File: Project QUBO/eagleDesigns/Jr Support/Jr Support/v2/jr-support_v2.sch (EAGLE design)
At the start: 254 parts, among them IC1 74LVC1G08DBV, IC2 TLC2272PW, IC3 74LVC1G08DBV, IC4 74LVC1G08DBV, Q1 FDN5618P, U1 PCA9685, U2 LT3063, U3 LT3063

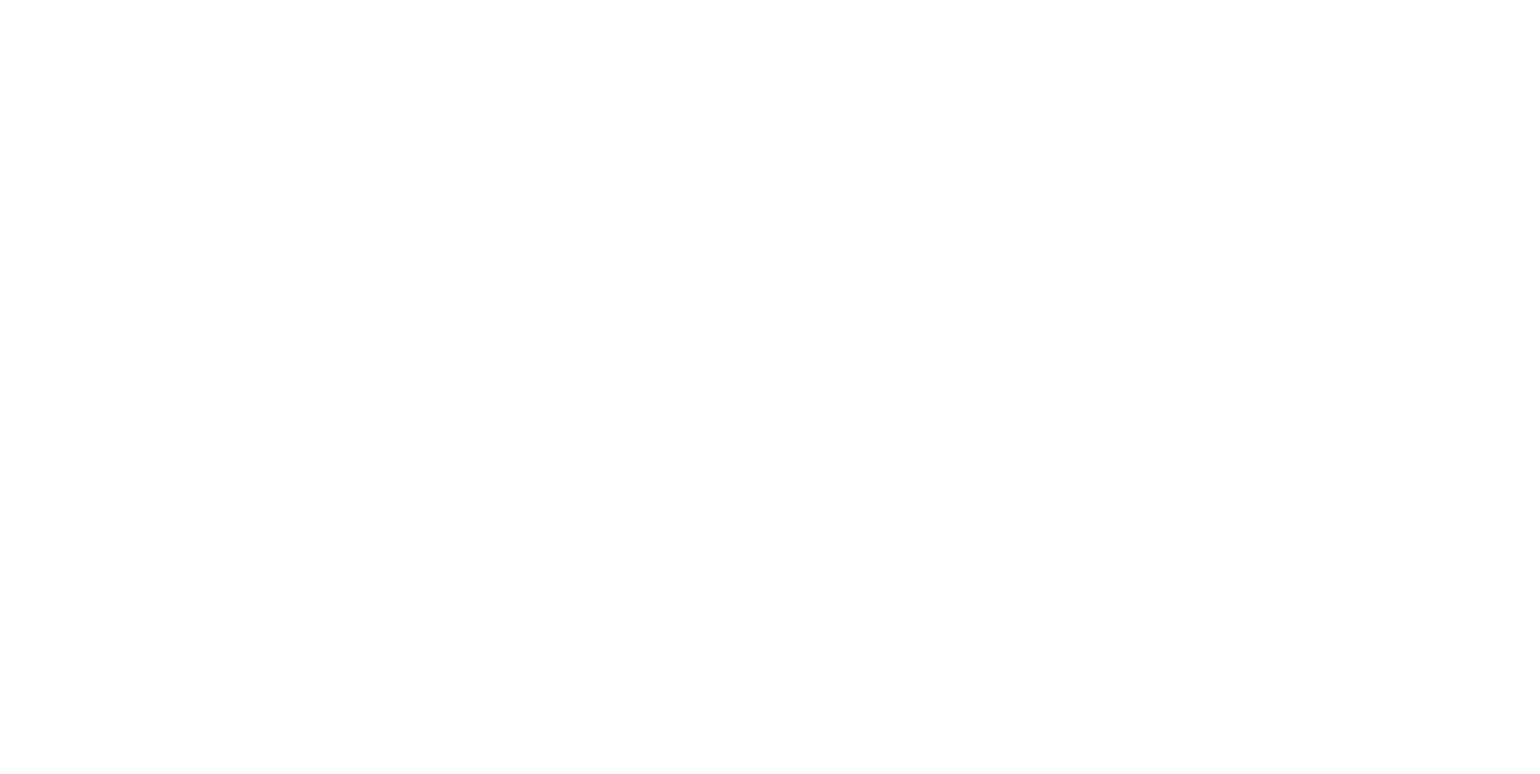
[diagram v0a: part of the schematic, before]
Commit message: 
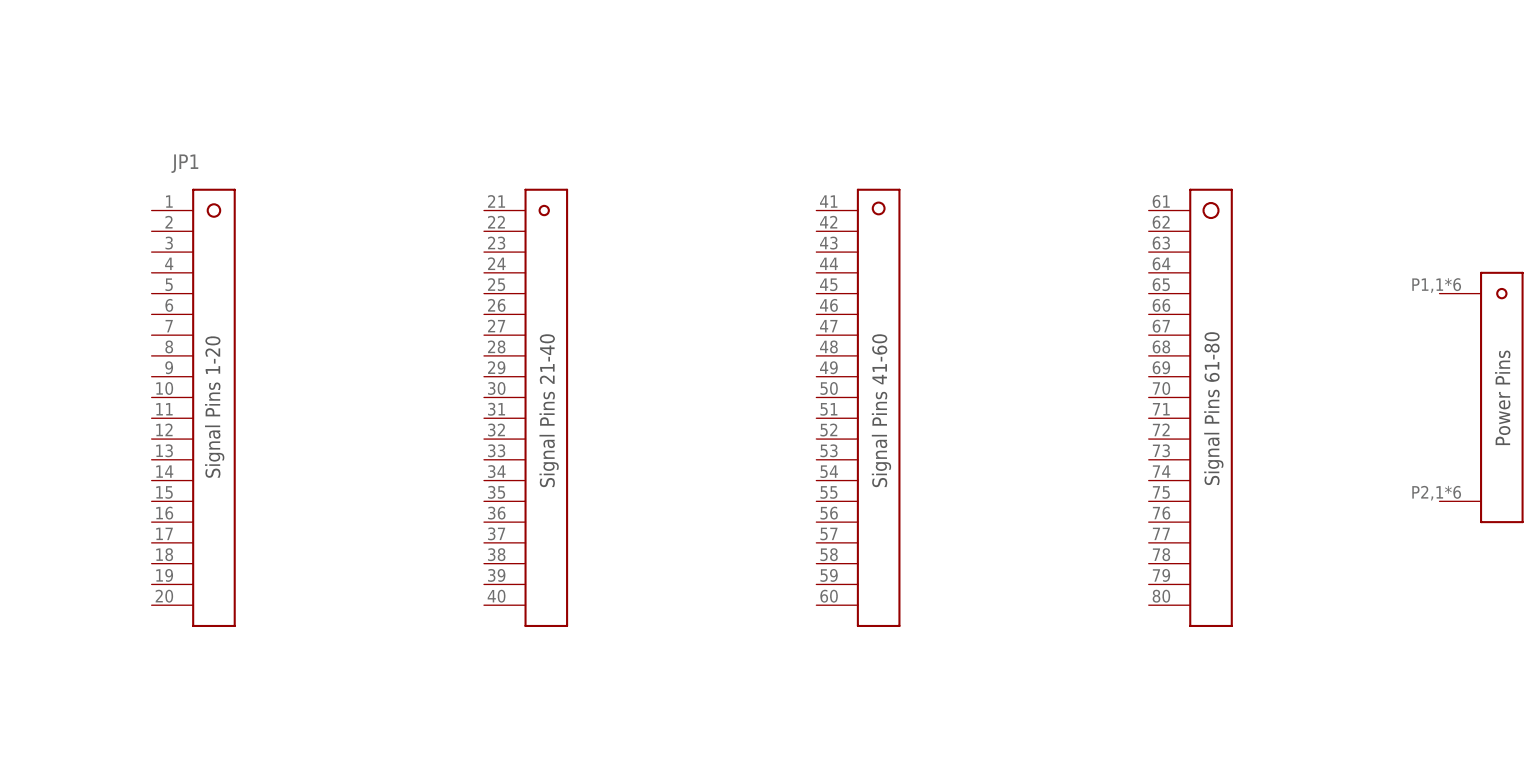
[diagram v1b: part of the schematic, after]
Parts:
- added JP1: (no value), samtec:MPSC-01-80MPSC-RA-LC
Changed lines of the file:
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@@
 <part name="R3" library="resistor" deviceset="R-US_" device="R0805" value="50k"/>
 <part name="5V_PG" library="led" deviceset="LED" device="CHIP-LED0805" value=" "/>
+<part name="JP1" library="samtec" deviceset="MPSC-01-80" device="MPSC-RA-LC"/>
 </parts>
 <sheets>
@@
 <instance part="R3" gate="G$1" x="-210.82" y="12.7" rot="R90"/>
 <instance part="5V_PG" gate="G$1" x="-231.14" y="-22.86"/>
+<instance part="JP1" gate="G$1" x="612.14" y="40.64"/>
 </instances>
 <busses>

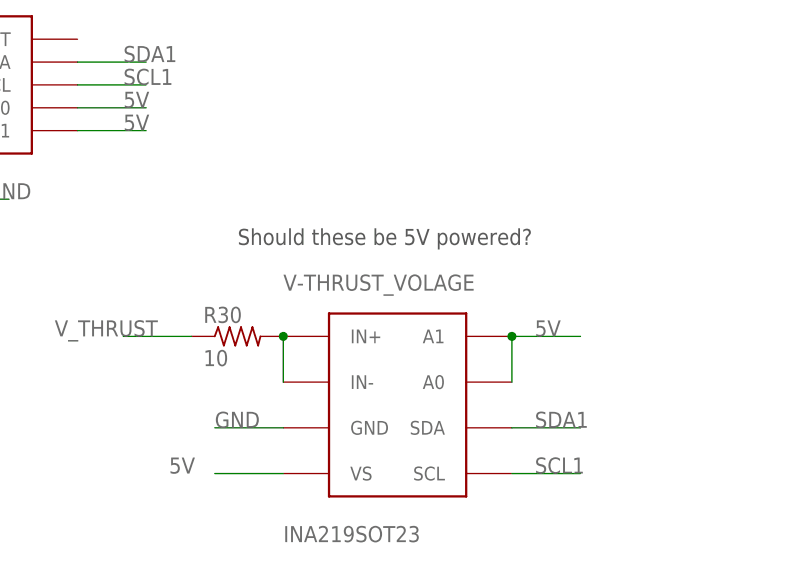
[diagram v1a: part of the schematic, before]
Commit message: 
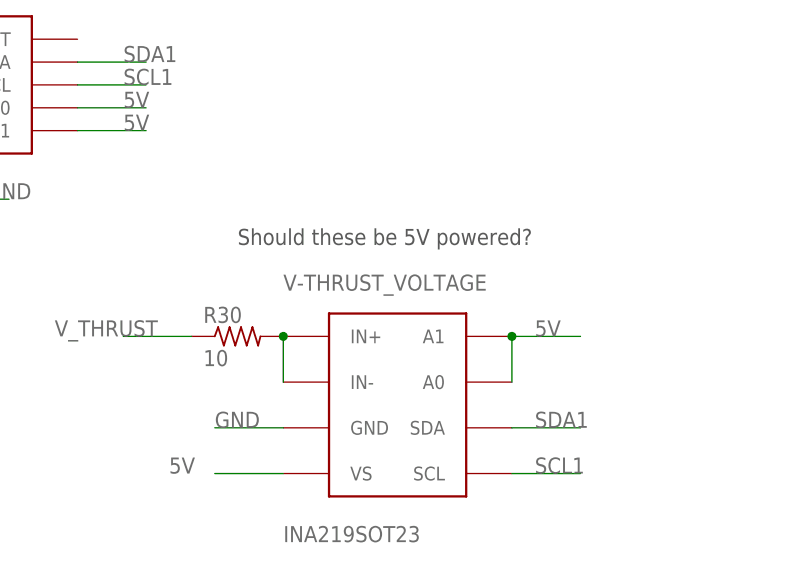
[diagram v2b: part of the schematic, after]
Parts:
- renumbered V-THRUST_VOLAGE to V-THRUST_VOLTAGE
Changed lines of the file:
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@@
 <?xml version="1.0" encoding="utf-8"?>
 <!DOCTYPE eagle SYSTEM "eagle.dtd">
-<eagle version="8.1.0">
+<eagle version="8.1.1">
 <drawing>
 <settings>
@@
 <part name="12V_VOLTAGE" library="texas" deviceset="INA219" device="SOT23"/>
 <part name="R25" library="resistor" deviceset="R-US_" device="R0805" value="10"/>
-<part name="V-THRUST_VOLAGE" library="texas" deviceset="INA219" device="SOT23"/>
+<part name="V-THRUST_VOLTAGE" library="texas" deviceset="INA219" device="SOT23"/>
 <part name="R30" library="resistor" deviceset="R-US_" device="R0805" value="10"/>
 <part name="5V_VOLTAGE" library="texas" deviceset="INA219" device="SOT23"/>
@@
 <instance part="12V_VOLTAGE" gate="G$1" x="53.34" y="109.22"/>
 <instance part="R25" gate="G$1" x="35.56" y="116.84"/>
-<instance part="V-THRUST_VOLAGE" gate="G$1" x="53.34" y="35.56"/>
+<instance part="V-THRUST_VOLTAGE" gate="G$1" x="53.34" y="35.56"/>
 <instance part="R30" gate="G$1" x="35.56" y="43.18"/>
 <instance part="5V_VOLTAGE" gate="G$1" x="53.34" y="-35.56"/>
@@
 </segment>
 <segment>
-<pinref part="V-THRUST_VOLAGE" gate="G$1" pin="GND"/>
+<pinref part="V-THRUST_VOLTAGE" gate="G$1" pin="GND"/>
 <wire x1="40.64" y1="33.02" x2="33.02" y2="33.02" width="0.1524" layer="91"/>
 <label x="33.02" y="33.02" size="1.778" layer="95"/>
@@
 </segment>
 <segment>
-<pinref part="V-THRUST_VOLAGE" gate="G$1" pin="VS"/>
+<pinref part="V-THRUST_VOLTAGE" gate="G$1" pin="VS"/>
 <wire x1="40.64" y1="27.94" x2="33.02" y2="27.94" width="0.1524" layer="91"/>
 <label x="27.94" y="27.94" size="1.778" layer="95"/>
@@
 </segment>
 <segment>
-<pinref part="V-THRUST_VOLAGE" gate="G$1" pin="A1"/>
+<pinref part="V-THRUST_VOLTAGE" gate="G$1" pin="A1"/>
 <wire x1="66.04" y1="43.18" x2="73.66" y2="43.18" width="0.1524" layer="91"/>
 <label x="68.58" y="43.18" size="1.778" layer="95"/>
-<pinref part="V-THRUST_VOLAGE" gate="G$1" pin="A0"/>
+<pinref part="V-THRUST_VOLTAGE" gate="G$1" pin="A0"/>
 <wire x1="66.04" y1="38.1" x2="66.04" y2="43.18" width="0.1524" layer="91"/>
 <junction x="66.04" y="43.18"/>
@@
 </segment>
 <segment>
-<pinref part="V-THRUST_VOLAGE" gate="G$1" pin="SCL"/>
+<pinref part="V-THRUST_VOLTAGE" gate="G$1" pin="SCL"/>
 <wire x1="66.04" y1="27.94" x2="73.66" y2="27.94" width="0.1524" layer="91"/>
 <label x="68.58" y="27.94" size="1.778" layer="95"/>
@@
 </segment>
 <segment>
-<pinref part="V-THRUST_VOLAGE" gate="G$1" pin="SDA"/>
+<pinref part="V-THRUST_VOLTAGE" gate="G$1" pin="SDA"/>
 <wire x1="66.04" y1="33.02" x2="73.66" y2="33.02" width="0.1524" layer="91"/>
 <label x="68.58" y="33.02" size="1.778" layer="95"/>
@@
 <net name="N$58" class="0">
 <segment>
-<pinref part="V-THRUST_VOLAGE" gate="G$1" pin="IN-"/>
-<pinref part="V-THRUST_VOLAGE" gate="G$1" pin="IN+"/>
+<pinref part="V-THRUST_VOLTAGE" gate="G$1" pin="IN-"/>
+<pinref part="V-THRUST_VOLTAGE" gate="G$1" pin="IN+"/>
 <wire x1="40.64" y1="38.1" x2="40.64" y2="43.18" width="0.1524" layer="91"/>
 <pinref part="R30" gate="G$1" pin="2"/>
